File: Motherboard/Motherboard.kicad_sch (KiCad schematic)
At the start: 6 parts

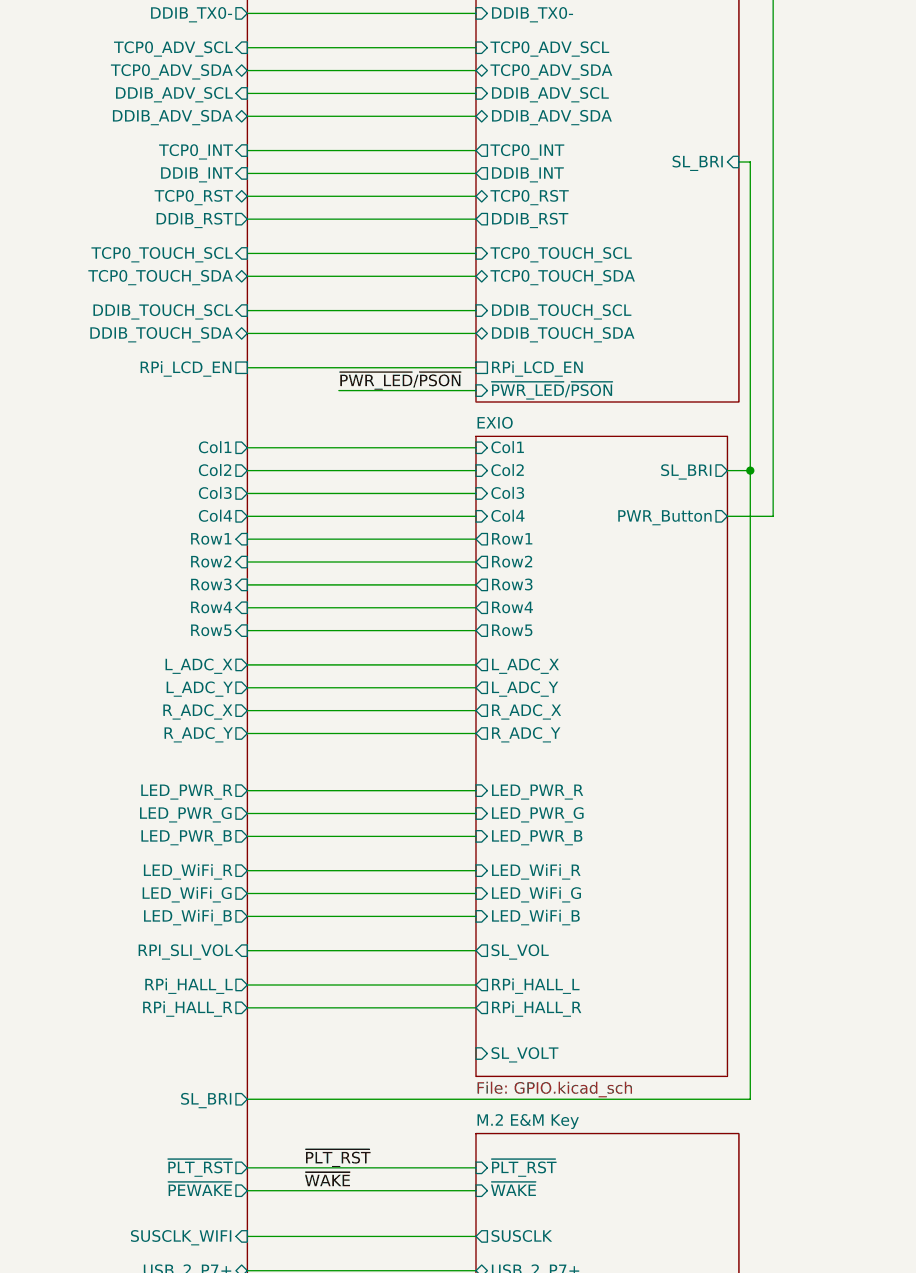
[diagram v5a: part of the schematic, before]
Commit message: Swapped Volume and Brightness sliders for easier wiring.
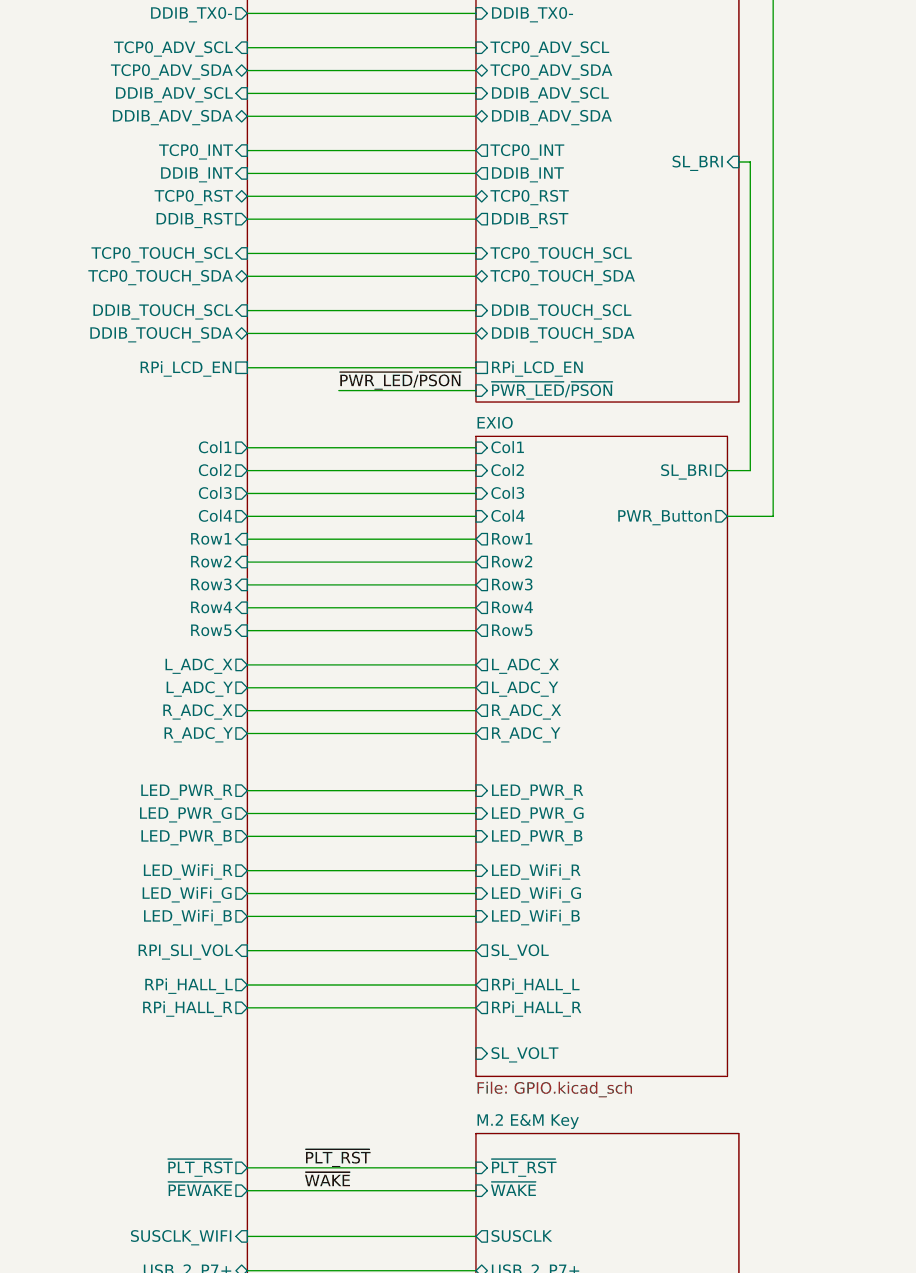
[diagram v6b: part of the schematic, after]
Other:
- sheet LattePanda Module ports: added none; removed SL_BRI
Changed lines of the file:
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@@
 		)
 	)
-	(junction
-		(at 410.21 198.12)
-		(diameter 0)
-		(color 0 0 0 0)
-	)
 	(no_connect
 		(at 180.34 278.13)
@@
 	(wire
 		(pts
-			(xy 410.21 198.12) (xy 410.21 267.97)
-		)
-		(stroke
-			(width 0)
-			(type default)
-		)
-	)
-	(wire
-		(pts
 			(xy 354.33 67.31) (xy 379.73 67.31)
 		)
@@
 	(wire
 		(pts
-			(xy 410.21 198.12) (xy 410.21 163.83)
+			(xy 410.21 163.83) (xy 410.21 198.12)
 		)
 		(stroke
@@
 	(wire
 		(pts
-			(xy 354.33 267.97) (xy 410.21 267.97)
+			(xy 354.33 156.21) (xy 379.73 156.21)
 		)
 		(stroke
@@
 	(wire
 		(pts
-			(xy 354.33 156.21) (xy 379.73 156.21)
+			(xy 354.33 114.3) (xy 379.73 114.3)
 		)
 		(stroke
@@
 	(wire
 		(pts
-			(xy 354.33 114.3) (xy 379.73 114.3)
+			(xy 354.33 300.99) (xy 379.73 300.99)
 		)
 		(stroke
@@
 	(wire
 		(pts
-			(xy 354.33 300.99) (xy 379.73 300.99)
+			(xy 354.33 203.2) (xy 379.73 203.2)
 		)
 		(stroke
@@
 	(wire
 		(pts
-			(xy 354.33 203.2) (xy 379.73 203.2)
+			(xy 208.28 298.45) (xy 240.03 298.45)
 		)
 		(stroke
@@
 	(wire
 		(pts
-			(xy 208.28 298.45) (xy 240.03 298.45)
+			(xy 407.67 198.12) (xy 410.21 198.12)
 		)
 		(stroke
@@
 	(wire
 		(pts
-			(xy 407.67 198.12) (xy 410.21 198.12)
-		)
-		(stroke
-			(width 0)
-			(type default)
-		)
-	)
-	(wire
-		(pts
 			(xy 354.33 74.93) (xy 379.73 74.93)
 		)
@@
 			(effects
 				(font
-					(size 1.27 1.27)
-				)
-				(justify right)
-			)
-		)
-		(pin "SL_BRI" output
-			(at 354.33 267.97 0)
-			(effects
-				(font

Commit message: Routed RP2354B, USB ports, rewired HDMI lanes to be cleaner, and many other fixes and improvements.
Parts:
- removed FID1, FID2: Fiducial, A_HDJ_Library:Fiducial_0.5mm_Mask1mm, symbol Mechanical:Fiducial
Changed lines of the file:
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@@
-	)
-	(symbol
-		(lib_id "Mechanical:Fiducial")
-		(at 473.71 360.68 0)
-		(unit 1)
-		(body_style 1)
-		(exclude_from_sim yes)
-		(in_bom no)
-		(on_board yes)
-		(in_pos_files yes)
-		(dnp no)
-		(fields_autoplaced yes)
-		(property "Reference" "FID1"
-			(at 476.25 359.41 0)
-			(show_name no)
-			(do_not_autoplace no)
-			(effects
-				(font
-					(size 1.27 1.27)
-				)
-				(justify left)
-			)
-		)
-		(property "Value" "Fiducial"
-			(at 476.25 361.95 0)
-			(show_name no)
-			(do_not_autoplace no)
-			(effects
-				(font
-					(size 1.27 1.27)
-				)
-				(justify left)
-			)
-		)
-		(property "Footprint" "A_HDJ_Library:Fiducial_0.5mm_Mask1mm"
-			(at 473.71 360.68 0)
-			(hide yes)
-			(show_name no)
-			(do_not_autoplace no)
-			(effects
-				(font
-					(size 1.27 1.27)
-				)
-			)
-		)
-		(property "Datasheet" ""
-			(at 473.71 360.68 0)
-			(hide yes)
-			(show_name no)
-			(do_not_autoplace no)
-			(effects
-				(font
-					(size 1.27 1.27)
-				)
-			)
-		)
-		(property "Description" ""
-			(at 473.71 360.68 0)
-			(hide yes)
-			(show_name no)
-			(do_not_autoplace no)
-			(effects
-				(font
-					(size 1.27 1.27)
-				)
-			)
-		)
-		(property "Sim.Device" ""
-			(at 473.71 360.68 0)
-			(hide yes)
-			(show_name no)
-			(do_not_autoplace no)
-			(effects
-				(font
-					(size 1.27 1.27)
-				)
-			)
-		)
-		(property "Sim.Pins" ""
-			(at 473.71 360.68 0)
-			(hide yes)
-			(show_name no)
-			(do_not_autoplace no)
-			(effects
-				(font
-					(size 1.27 1.27)
-				)
-			)
-		)
-		(property "Sim.Type" ""
-			(at 473.71 360.68 0)
-			(hide yes)
-			(show_name no)
-			(do_not_autoplace no)
-			(effects
-				(font
-					(size 1.27 1.27)
-				)
-			)
-		)
-		(property "Field-1" ""
-			(at 0 721.36 0)
-			(hide yes)
-			(show_name no)
-			(do_not_autoplace no)
-			(effects
-				(font
-					(size 1.27 1.27)
-				)
-			)
-		)
-		(instances
-			(project "Motherboard"
-				(path "/2a6d114a-7fd7-4207-b5f7-4ea9c34f36aa"
-					(reference "FID1")
-					(unit 1)
-				)
-			)
-		)
-	)
-	(symbol
-		(lib_id "Mechanical:Fiducial")
-		(at 473.71 365.76 0)
-		(unit 1)
-		(body_style 1)
-		(exclude_from_sim yes)
-		(in_bom no)
-		(on_board yes)
-		(in_pos_files yes)
-		(dnp no)
-		(fields_autoplaced yes)
-		(property "Reference" "FID2"
-			(at 476.25 364.49 0)
-			(show_name no)
-			(do_not_autoplace no)
-			(effects
-				(font
-					(size 1.27 1.27)
-				)
-				(justify left)
-			)
-		)
-		(property "Value" "Fiducial"
-			(at 476.25 367.03 0)
-			(show_name no)
-			(do_not_autoplace no)
-			(effects
-				(font
-					(size 1.27 1.27)
-				)
-				(justify left)
-			)
-		)
-		(property "Footprint" "A_HDJ_Library:Fiducial_0.5mm_Mask1mm"
-			(at 473.71 365.76 0)
-			(hide yes)
-			(show_name no)
-			(do_not_autoplace no)
-			(effects
-				(font
-					(size 1.27 1.27)
-				)
-			)
-		)
-		(property "Datasheet" ""
-			(at 473.71 365.76 0)
-			(hide yes)
-			(show_name no)
-			(do_not_autoplace no)
-			(effects
-				(font
-					(size 1.27 1.27)
-				)
-			)
-		)
-		(property "Description" ""
-			(at 473.71 365.76 0)
-			(hide yes)
-			(show_name no)
-			(do_not_autoplace no)
-			(effects
-				(font
-					(size 1.27 1.27)
-				)
-			)
-		)
-		(property "Sim.Device" ""
-			(at 473.71 365.76 0)
-			(hide yes)
-			(show_name no)
-			(do_not_autoplace no)
-			(effects
-				(font
-					(size 1.27 1.27)
-				)
-			)
-		)
-		(property "Sim.Pins" ""
-			(at 473.71 365.76 0)
-			(hide yes)
-			(show_name no)
-			(do_not_autoplace no)
-			(effects
-				(font
-					(size 1.27 1.27)
-				)
-			)
-		)
-		(property "Sim.Type" ""
-			(at 473.71 365.76 0)
-			(hide yes)
-			(show_name no)
-			(do_not_autoplace no)
-			(effects
-				(font
-					(size 1.27 1.27)
-				)
-			)
-		)
-		(property "Field-1" ""
-			(at 0 731.52 0)
-			(hide yes)
-			(show_name no)
-			(do_not_autoplace no)
-			(effects
-				(font
-					(size 1.27 1.27)
-				)
-			)
-		)
-		(instances
-			(project "Motherboard"
-				(path "/2a6d114a-7fd7-4207-b5f7-4ea9c34f36aa"
-					(reference "FID2")
-					(unit 1)
-				)
-			)
-		)
 	)
 	(symbol

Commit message: Created updated BOM for PCBWay on all CTRL daughterboards. These boards have likely hit their final* version
*Ive said "Finished Version" many times in this project. I'm confident now, but no guarantees.
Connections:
- no-connect marks 5 -> 7
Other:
- sheet EXIO ports: added none; removed SL_VOLT
